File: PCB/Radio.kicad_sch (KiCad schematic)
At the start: 31 parts, among them J701 Conn_Coaxial, U701 SX1262, U702 SKY13453-385LF, Y701 NX2016SA-32MHZ-STD-CZS-5

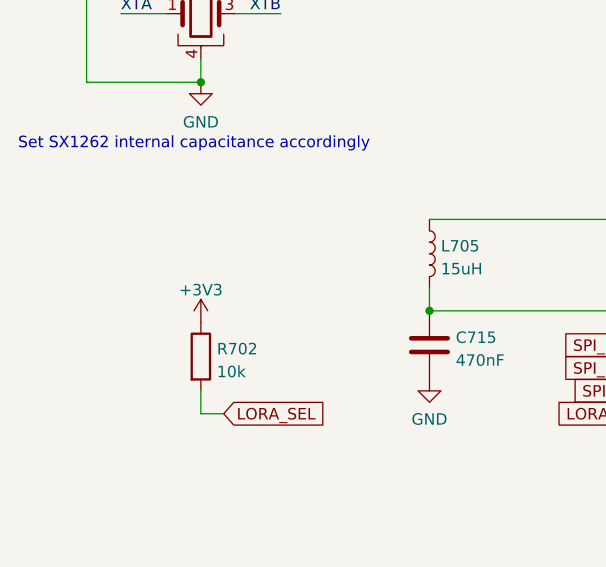
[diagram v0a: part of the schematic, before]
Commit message: Made sensors use SPI instead of I2C Change external I2C connector to qwiic Made SWD have its own pin header
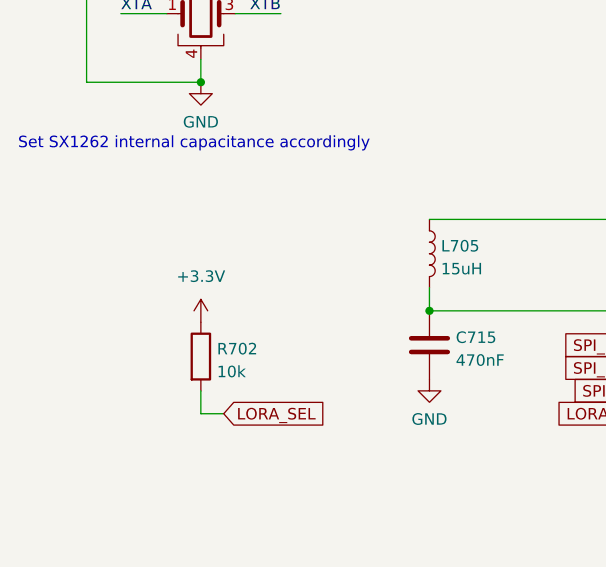
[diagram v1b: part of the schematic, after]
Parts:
- J701: footprint Connector_Coaxial:SMA_Amphenol_132134-11_Vertical -> Connector_Coaxial:SMA_Samtec_SMA-J-P-H-ST-EM1_EdgeMount
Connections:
- net +3V3 is gone; now on net +3.3V: R702.1
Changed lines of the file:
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@@
 			)
 		)
-		(property "Footprint" "Connector_Coaxial:SMA_Amphenol_132134-11_Vertical"
+		(property "Footprint" "Connector_Coaxial:SMA_Samtec_SMA-J-P-H-ST-EM1_EdgeMount"
 			(at 271.78 92.71 0)
 			(effects
@@
 			)
 		)
-		(property "Value" "+3V3"
-			(at 46.99 106.9142 0)
-			(effects
-				(font
+		(property "Value" "+3.3V"
+			(at 46.99 105.41 0)
+			(effects
+				(font
